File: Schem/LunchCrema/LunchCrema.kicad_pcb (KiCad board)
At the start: 4 copper layers, 160 x 64.4 mm, 53 parts, among them IC1 MMPQ3904, J1 pBITzBus, J3 DE15_Socket_HighDensity_Mount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, SW1 SW_Coded_SH-7070, U1 74HC688, U10 74HC139, U2 V9958, U3 74HC273, U8 74LVC1G19, U9 BAT54JW-7-F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

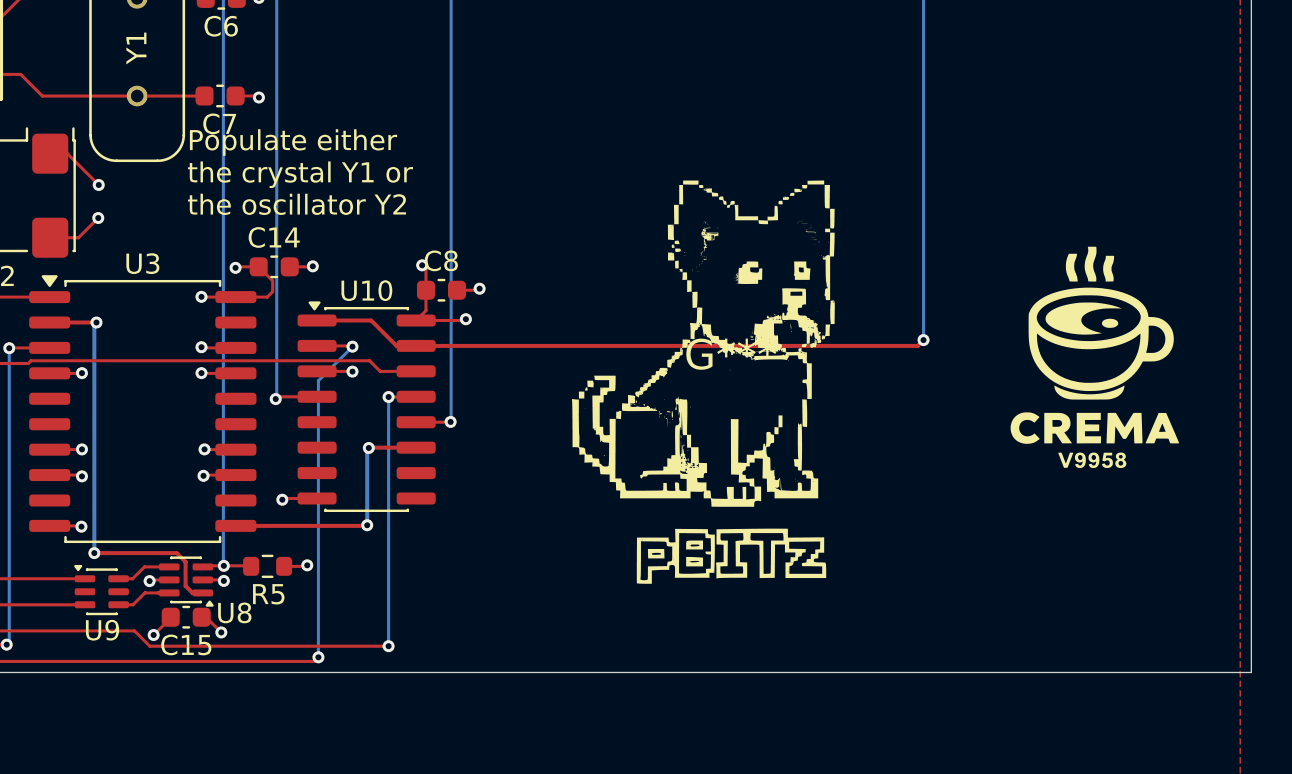
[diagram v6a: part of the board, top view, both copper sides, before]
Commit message: Fixed an issue with the pBITz Interface connector where pinout was reversed. Generated the images, pdf and production files for the LunchCrema PCB.
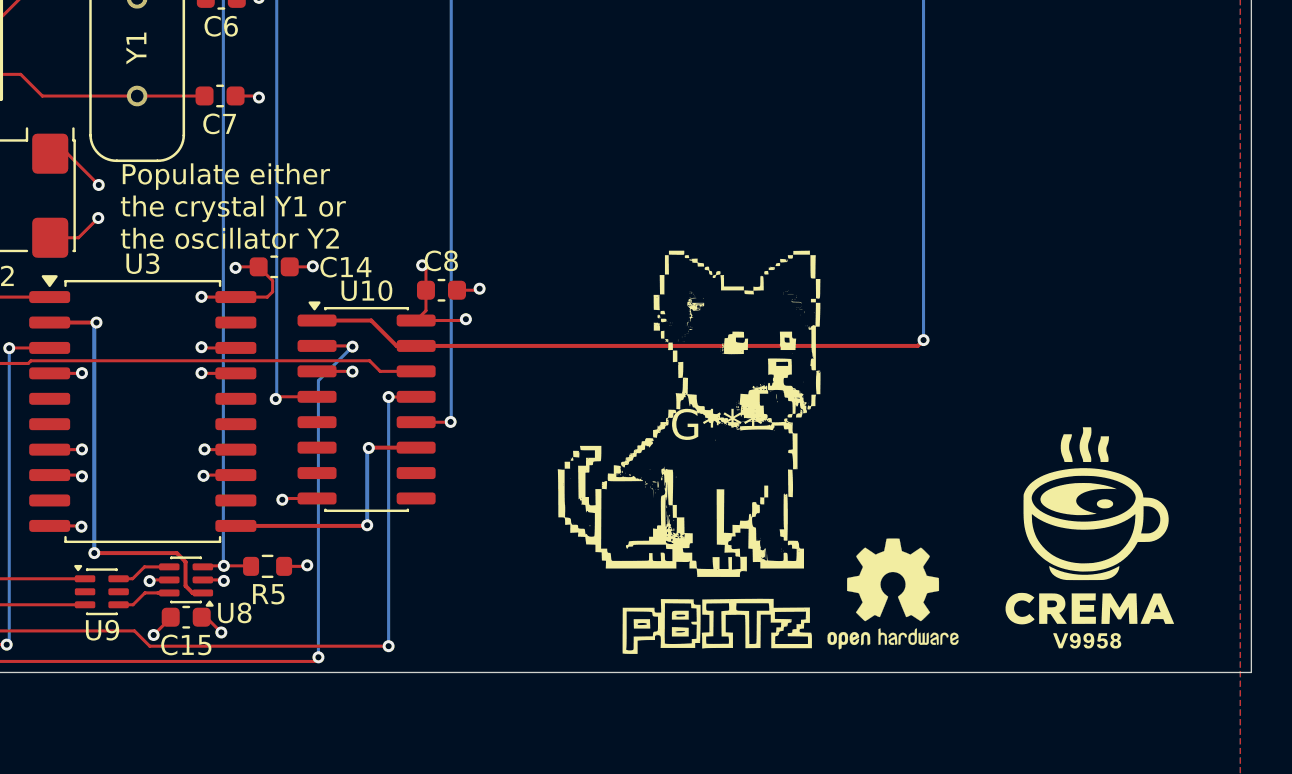
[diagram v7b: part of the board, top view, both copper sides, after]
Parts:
- added REF**: OSHW-Logo2_7.3x6mm_SilkScreen, Symbol:OSHW-Logo2_7.3x6mm_SilkScreen, F.Cu at (406.3, 168.2)
- moved G*** 9.02 mm to (415.9, 165.5)
- moved G*** 3.58 mm to (397.4, 159.8)
